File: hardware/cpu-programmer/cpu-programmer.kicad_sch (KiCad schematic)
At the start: 14 parts, among them J1 Conn_01x15_Socket, J2 Conn_01x04_Socket, SW1 Boot, SW2 Write, U1 CH32X033F8P6

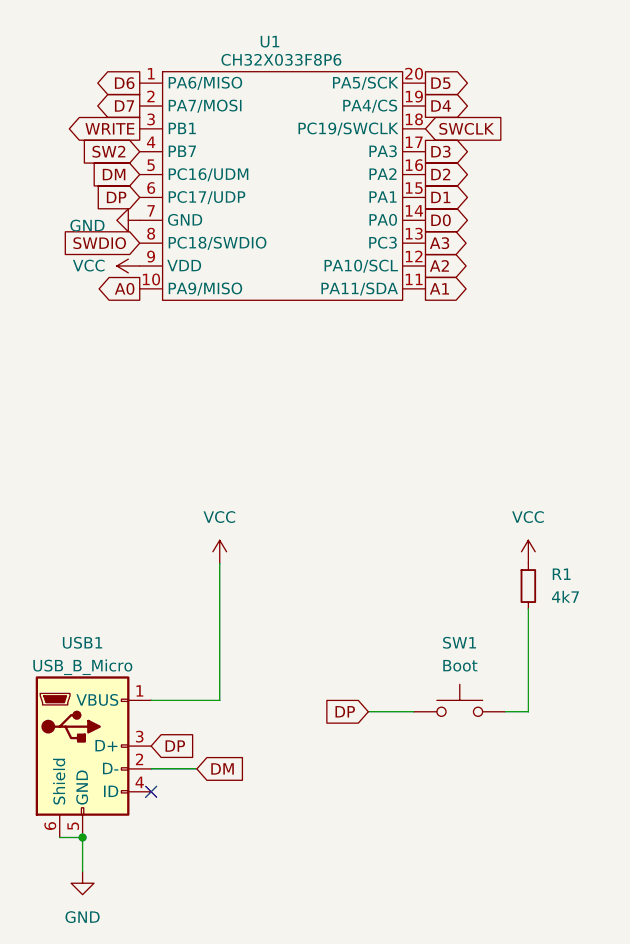
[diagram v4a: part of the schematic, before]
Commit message: Fixed differential pair
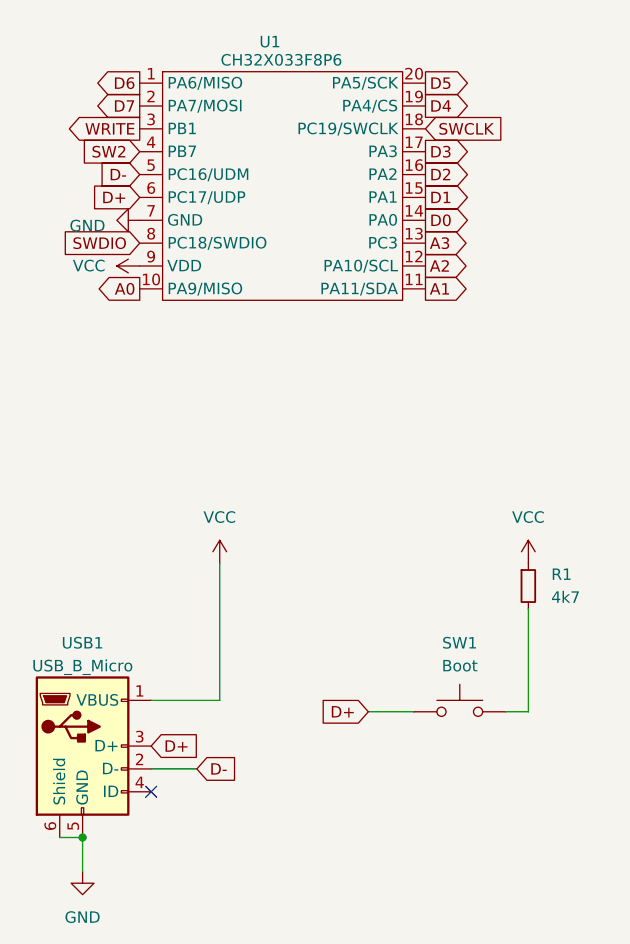
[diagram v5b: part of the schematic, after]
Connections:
- net DM renamed D-
- net DP renamed D+
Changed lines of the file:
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@@
 		)
 	)
-	(global_label "DM"
+	(global_label "D-"
 		(shape input)
 		(at 34.29 41.91 180)
@@
 		)
 		(property "Intersheetrefs" "${INTERSHEET_REFS}"
-			(at 28.6628 41.91 0)
-			(effects
-				(font
-					(size 1.27 1.27)
-				)
-				(justify right)
-				(hide yes)
-			)
-		)
-	)
-	(global_label "DP"
+			(at 28.4624 41.91 0)
+			(effects
+				(font
+					(size 1.27 1.27)
+				)
+				(justify right)
+				(hide yes)
+			)
+		)
+	)
+	(global_label "D+"
 		(shape input)
 		(at 35.56 105.41 0)
@@
 		)
 		(property "Intersheetrefs" "${INTERSHEET_REFS}"
-			(at 41.0058 105.41 0)
+			(at 41.3876 105.41 0)
 			(effects
 				(font
@@
 		)
 	)
-	(global_label "DM"
+	(global_label "D-"
 		(shape input)
 		(at 40.64 107.95 0)
@@
 		)
 		(property "Intersheetrefs" "${INTERSHEET_REFS}"
-			(at 46.2672 107.95 0)
+			(at 46.4676 107.95 0)
 			(effects
 				(font
@@
 		)
 	)
-	(global_label "DP"
+	(global_label "D+"
 		(shape input)
 		(at 59.69 101.6 180)
@@
 		)
 		(property "Intersheetrefs" "${INTERSHEET_REFS}"
-			(at 54.1648 101.6 0)
+			(at 53.8624 101.6 0)
 			(effects
 				(font
@@
 		)
 	)
-	(global_label "DP"
+	(global_label "D+"
 		(shape input)
 		(at 34.29 44.45 180)
@@
 		)
 		(property "Intersheetrefs" "${INTERSHEET_REFS}"
-			(at 28.8442 44.45 0)
-			(effects
-				(font
+			(at 28.4624 44.45 0)
+			(effects
+				(font
